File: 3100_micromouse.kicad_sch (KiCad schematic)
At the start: 11 parts

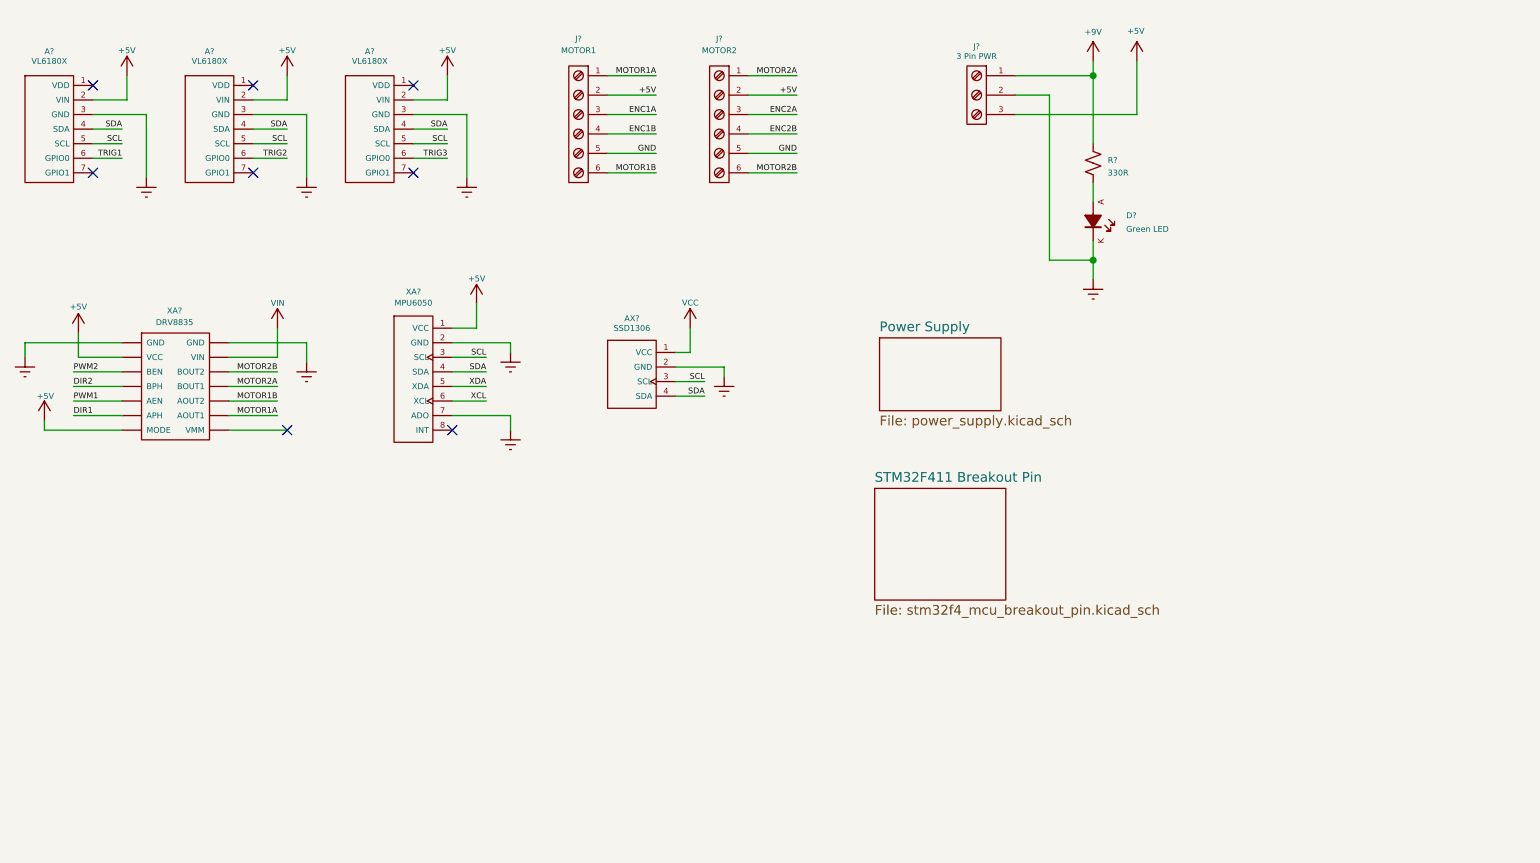
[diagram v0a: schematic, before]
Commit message: Added Footprint model for all components except connectors
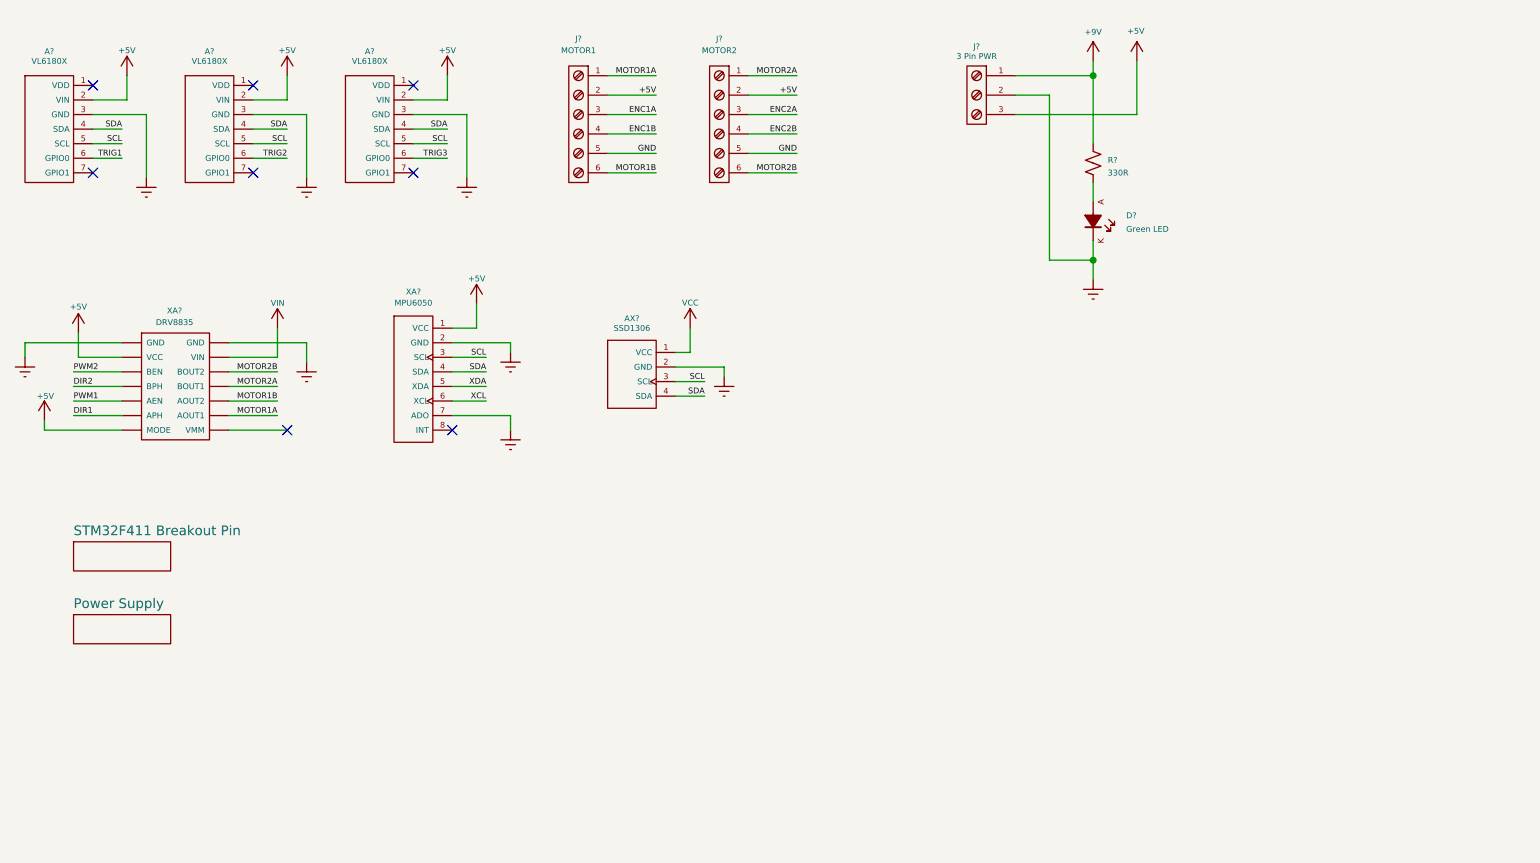
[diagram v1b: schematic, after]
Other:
- title: (none) -> MTRN3100 Micromouse
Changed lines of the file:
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@@
 	(generator_version "9.0")
 	(paper "A5")
+	(title_block
+		(title "MTRN3100 Micromouse")
+		(date "2025-06-20")
+		(rev "1.0")
+	)
 	(junction
 		(at 161.29 50.8)
@@
 	)
 	(sheet
-		(at 132.715 80.645)
-		(size 17.145 14.605)
+		(at 27.94 87.63)
+		(size 12.7 3.81)
 		(exclude_from_sim no)
 		(in_bom yes)
@@
 		)
 		(property "Sheetname" "STM32F411 Breakout Pin"
-			(at 132.715 79.9334 0)
+			(at 27.94 86.9184 0)
 			(effects
 				(font
@@
 		)
 		(property "Sheetfile" "stm32f4_mcu_breakout_pin.kicad_sch"
-			(at 132.715 95.8346 0)
+			(at 27.94 92.0246 0)
 			(effects
 				(font
@@
 				)
 				(justify left top)
+				(hide yes)
 			)
 		)
@@
 	)
 	(sheet
-		(at 133.35 60.96)
-		(size 15.875 9.525)
+		(at 27.94 97.155)
+		(size 12.7 3.81)
 		(exclude_from_sim no)
 		(in_bom yes)
@@
 		)
 		(property "Sheetname" "Power Supply"
-			(at 133.35 60.2484 0)
+			(at 27.94 96.4434 0)
 			(effects
 				(font
@@
 		)
 		(property "Sheetfile" "power_supply.kicad_sch"
-			(at 133.35 71.0696 0)
+			(at 27.94 101.5496 0)
 			(effects
 				(font
@@
 				)
 				(justify left top)
+				(hide yes)
 			)
 		)

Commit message: Finished All footprints - PCB placement done momemtarily - plus wiring buck convertor done
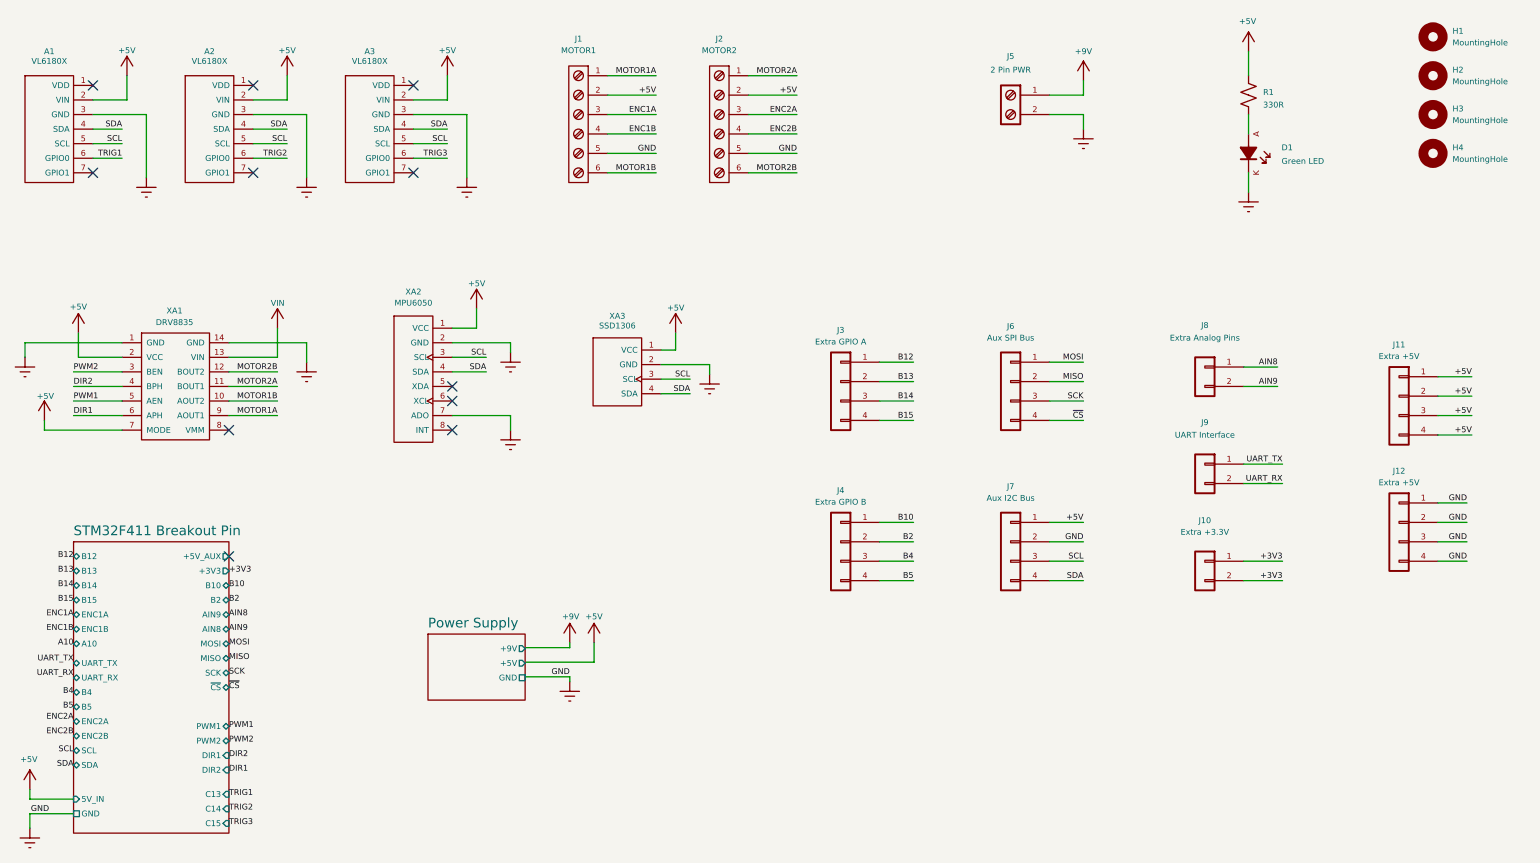
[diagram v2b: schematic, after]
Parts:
- added H1, H2, H3, H4: MountingHole, MountingHole:MountingHole_3.2mm_M3, symbol Mechanical:MountingHole
- added J10: Extra +3.3V, Connector_PinSocket_2.54mm:PinSocket_1x02_P2.54mm_Vertical, symbol Connector_Generic:Conn_01x02
- added J11, J12: Extra +5V, Connector_PinSocket_2.54mm:PinSocket_1x04_P2.54mm_Vertical, symbol Connector_Generic:Conn_01x04
- added J3: Extra GPIO A, Connector_PinSocket_2.54mm:PinSocket_1x04_P2.54mm_Vertical, symbol Connector_Generic:Conn_01x04
- added J4: Extra GPIO B, Connector_PinSocket_2.54mm:PinSocket_1x04_P2.54mm_Vertical, symbol Connector_Generic:Conn_01x04
- added J6: Aux SPI Bus, Connector_PinSocket_2.54mm:PinSocket_1x04_P2.54mm_Vertical, symbol Connector_Generic:Conn_01x04
- added J7: Aux I2C Bus, Connector_PinSocket_2.54mm:PinSocket_1x04_P2.54mm_Vertical, symbol Connector_Generic:Conn_01x04
- added J8: Extra Analog Pins, Connector_PinSocket_2.54mm:PinSocket_1x02_P2.54mm_Vertical, symbol Connector_Generic:Conn_01x02
- added J9: UART Interface, Connector_PinSocket_2.54mm:PinSocket_1x02_P2.54mm_Vertical, symbol Connector_Generic:Conn_01x02
- A1, A2, A3: renamed from A?; footprint (none) -> Library:VL6180X_Module_Vertical
- J1, J2: renamed from J?; footprint TerminalBlock_TE-Connectivity:TerminalBlock_TE_282834-6_1x06_P2.54mm_Horizontal -> Library:TE_Terminal_3.81_6P
- J5: renamed from J?; value 3 Pin PWR -> 2 Pin PWR; footprint 4ms_Connector:Pins_1x03_2.54mm_TH_AudioInsRGndL -> Library:KEFA_KF2EDGR_3.81_2P; symbol Connector:Screw_Terminal_01x03 -> Connector:Screw_Terminal_01x02
- R1: renamed from R?; footprint PCM_Resistor_THT_AKL:R_Axial_DIN0411_L9.9mm_D3.6mm_P12.70mm_Horizontal -> PCM_Resistor_THT_AKL:R_Axial_DIN0207_L6.3mm_D2.5mm_P10.16mm_Horizontal
- XA1: renamed from XA?; footprint (none) -> Library:DRV8835_Module
- XA2: renamed from XA?; footprint (none) -> Library:MPU6050_Module
- XA3: renamed from AX?; footprint (none) -> Library:SSD1306_OLED_Module
- gave numbers to parts that had none: 1
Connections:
- net GND is gone; now on net GNDREF: J1.5 (Pin_5), J2.5 (Pin_5)
- net VCC is gone; now on net +5V: XA3.1 (VCC)
- net +5V: now also R1.1, XA1.2 (VCC), XA1.7 (MODE), J11.1 (Pin_1), J11.2 (Pin_2), J11.3 (Pin_3), J11.4 (Pin_4), J7.1 (Pin_1); no longer J5.3 (Pin_3), XA1. (VMM)
- net +9V: no longer R1.1
- net DIR1: now also XA1.6 (APH); no longer XA1. (VMM)
- net DIR2: now also XA1.4 (BPH); no longer XA1. (VMM)
- net GNDREF: now also XA1.1 (GND), XA1.14 (GND), J12.1 (Pin_1), J12.2 (Pin_2), J12.3 (Pin_3), J12.4 (Pin_4), J7.2 (Pin_2); no longer XA1. (VMM)
- net MOTOR1A: now also XA1.9 (AOUT1); no longer XA1. (VMM)
- net MOTOR1B: now also XA1.10 (AOUT2); no longer XA1. (VMM)
- net MOTOR2A: now also XA1.11 (BOUT1); no longer XA1. (VMM)
- net MOTOR2B: now also XA1.12 (BOUT2); no longer XA1. (VMM)
- net PWM1: now also XA1.5 (AEN); no longer XA1. (VMM)
- net PWM2: now also XA1.3 (BEN); no longer XA1. (VMM)
- net SCL: now also J7.3 (Pin_3)
- net SDA: now also J7.4 (Pin_4)
- net VIN: now also XA1.13 (VIN); no longer XA1. (VMM)
- net XCL: no longer names the net of XA2.6 (XCL)
- net XDA: no longer names the net of XA2.5 (XDA)
- new net +3V3: J10.1 (Pin_1), J10.2 (Pin_2)
- new net AIN8: J8.1 (Pin_1)
- new net AIN9: J8.2 (Pin_2)
- new net B10: J4.1 (Pin_1)
- new net B12: J3.1 (Pin_1)
- new net B13: J3.2 (Pin_2)
- new net B14: J3.3 (Pin_3)
- new net B15: J3.4 (Pin_4)
- new net B2: J4.2 (Pin_2)
- new net B4: J4.3 (Pin_3)
- new net B5: J4.4 (Pin_4)
- new net MISO: J6.2 (Pin_2)
- new net MOSI: J6.1 (Pin_1)
- new net SCK: J6.3 (Pin_3)
- new net UART_RX: J9.2 (Pin_2)
- new net UART_TX: J9.1 (Pin_1)
- new net ~{CS}: J6.4 (Pin_4)
- no-connect marks 8 -> 11
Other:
- sheet Power Supply ports: added +5V, +9V, GND; removed none
- sheet STM32F411 Breakout Pin ports: added +3V3, +5V_AUX, 5V_IN, A10, AIN8, AIN9, B10, B12, B13, B14, B15, B2, B4, B5, C13, C14, C15, DIR1, DIR2, ENC1A, ENC1B, ENC2A, ENC2B, GND, MISO, MOSI, PWM1, PWM2, SCK, SCL, SDA, UART_RX, UART_TX, ~{CS}; removed none
- moved on the sheet: D1, R1, XA3

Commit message: Changed TOF Trigger pins to B12-14 - also removed 3V3 access as board space are running out
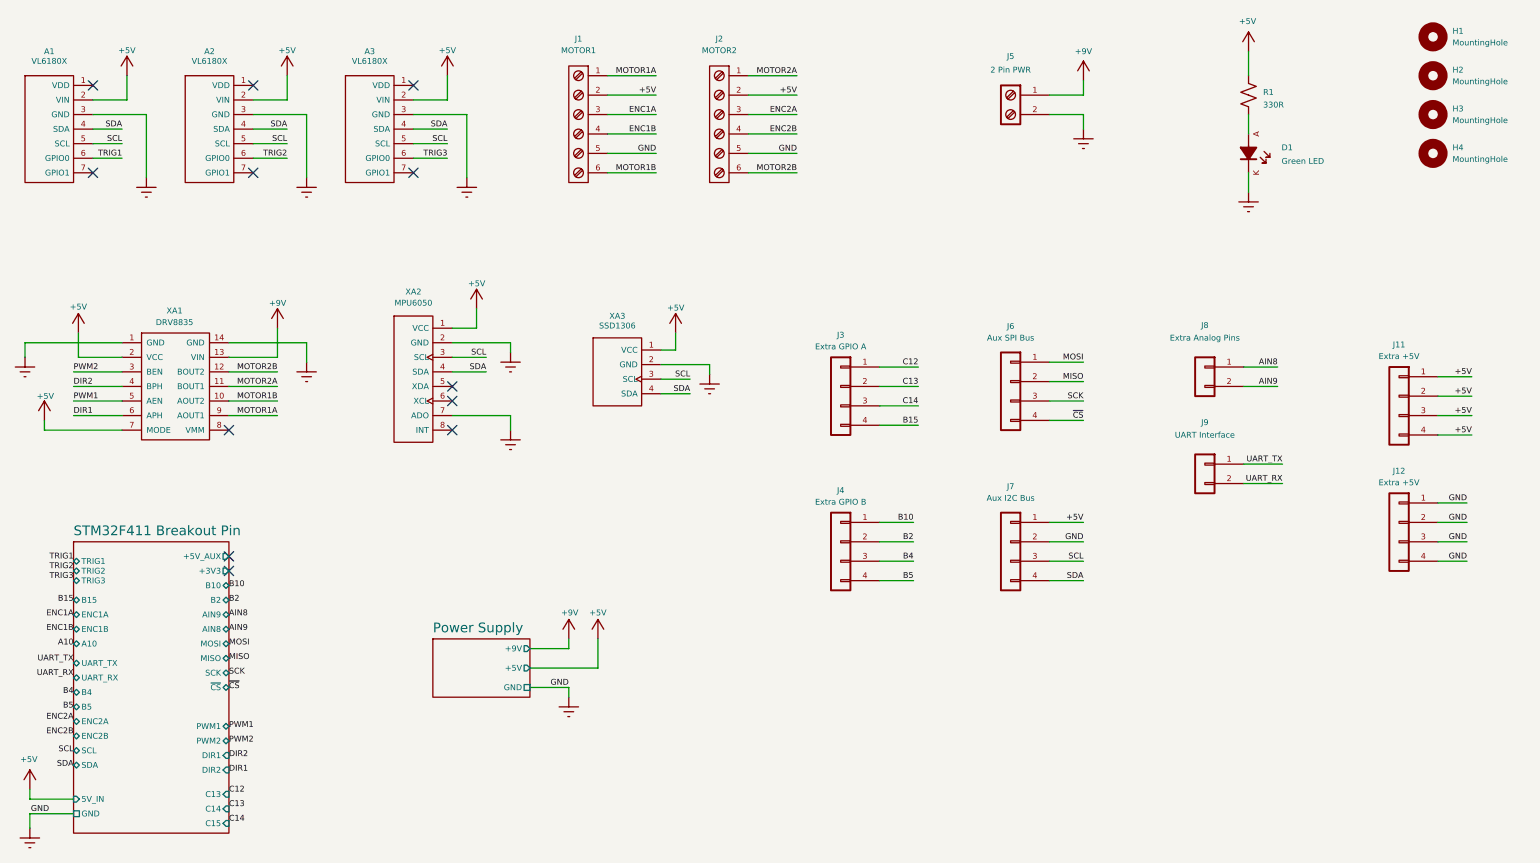
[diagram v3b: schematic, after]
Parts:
- removed J10: Extra +3.3V, Connector_PinSocket_2.54mm:PinSocket_1x02_P2.54mm_Vertical, symbol Connector_Generic:Conn_01x02
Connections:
- net VIN is gone; now on net +9V: XA1.13 (VIN)
- net B12 renamed C12
- net B13 renamed C13
- net B14 renamed C14
- no-connect marks 11 -> 12
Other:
- sheet STM32F411 Breakout Pin ports: added TRIG1, TRIG2, TRIG3; removed B12, B13, B14
- moved on the sheet: J3
